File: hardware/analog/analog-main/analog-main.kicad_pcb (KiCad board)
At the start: 2 copper layers, 3 parts

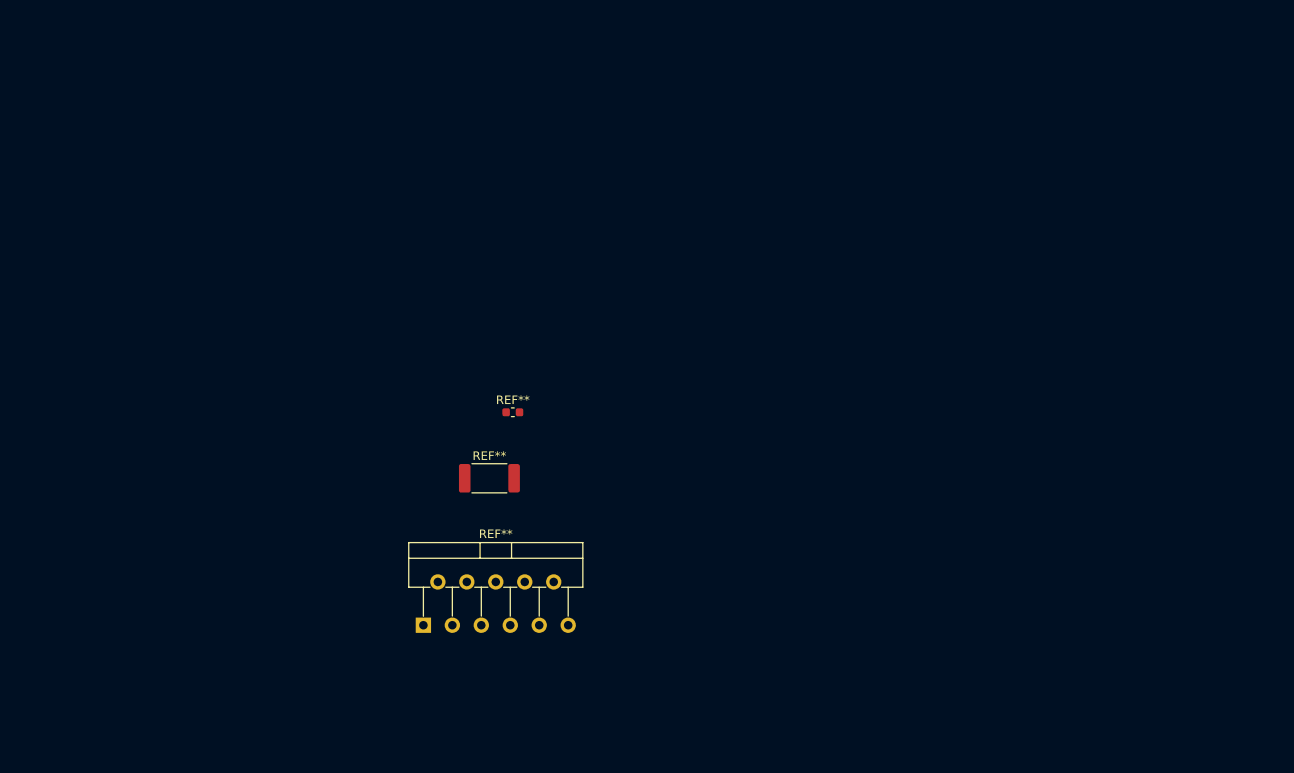
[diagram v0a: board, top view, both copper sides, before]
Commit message: Started work on Analog Main (Power Supply) board
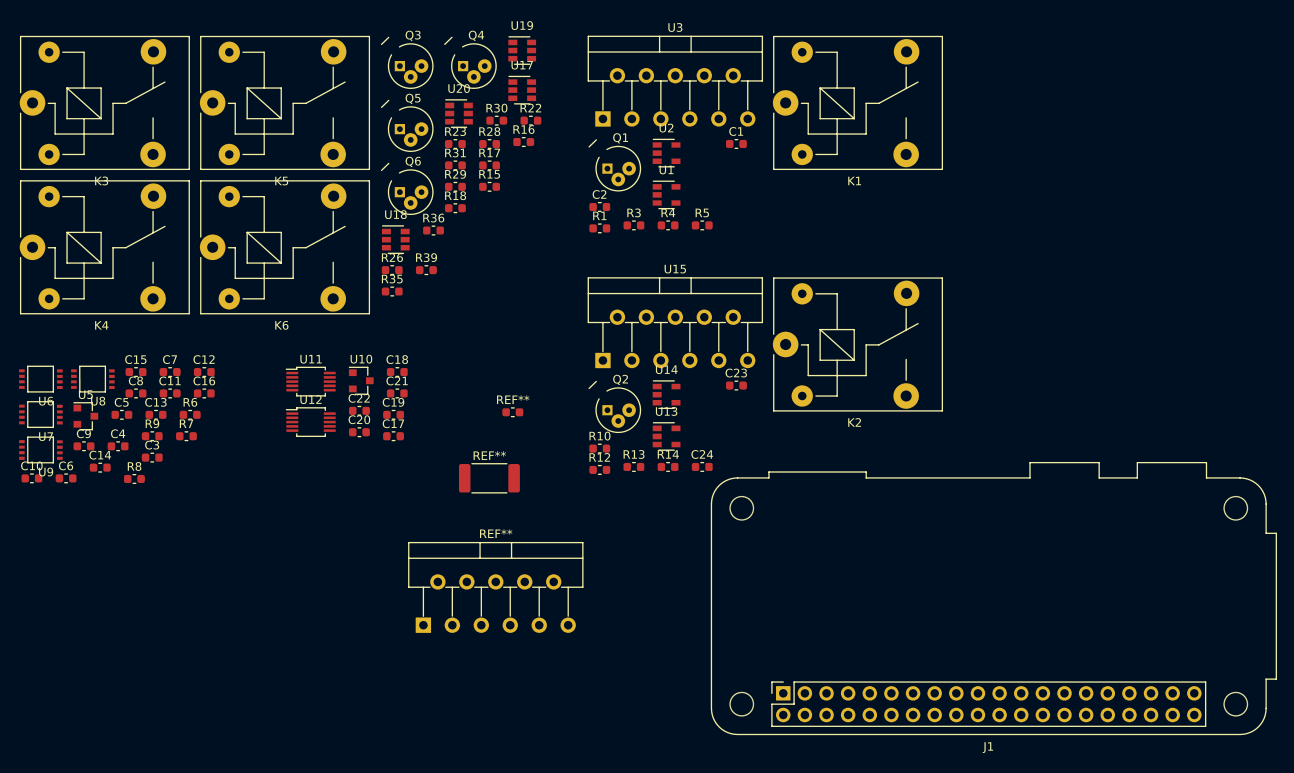
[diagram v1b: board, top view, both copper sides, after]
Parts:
- added C1: 100n, Capacitor_SMD:C_0603_1608Metric, F.Cu at (165.5, 46.5)
- added C10: 100n, Capacitor_SMD:C_0603_1608Metric, F.Cu at (82.8, 85.8)
- added C11: 100n / 100p, Capacitor_SMD:C_0603_1608Metric, F.Cu at (99.0, 75.8)
- added C12: 100n / 100p, Capacitor_SMD:C_0603_1608Metric, F.Cu at (103.0, 73.3)
- added C13: 4u7, Capacitor_SMD:C_0603_1608Metric, F.Cu at (97.4, 78.3)
- added C14: 4u7, Capacitor_SMD:C_0603_1608Metric, F.Cu at (90.8, 84.5)
- added C15: 100n, Capacitor_SMD:C_0603_1608Metric, F.Cu at (95.0, 73.3)
- added C16: 100n, Capacitor_SMD:C_0603_1608Metric, F.Cu at (103.0, 75.8)
- added C17: 100n, Capacitor_SMD:C_0603_1608Metric, F.Cu at (125.2, 80.8)
- added C18: 100n, Capacitor_SMD:C_0603_1608Metric, F.Cu at (125.7, 73.3)
- added C19: 100n, Capacitor_SMD:C_0603_1608Metric, F.Cu at (125.2, 78.3)
- added C2: 100n, Capacitor_SMD:C_0603_1608Metric, F.Cu at (149.5, 53.9)
- added C20: 100n, Capacitor_SMD:C_0603_1608Metric, F.Cu at (121.2, 80.3)
- added C21: 100n, Capacitor_SMD:C_0603_1608Metric, F.Cu at (125.7, 75.8)
- added C22: 100n, Capacitor_SMD:C_0603_1608Metric, F.Cu at (121.2, 77.8)
- added C23: 100n, Capacitor_SMD:C_0603_1608Metric, F.Cu at (165.5, 74.9)
- added C24: 100n, Capacitor_SMD:C_0603_1608Metric, F.Cu at (161.5, 84.4)
- added C3: 100n / 100p, Capacitor_SMD:C_0603_1608Metric, F.Cu at (96.9, 83.3)
- added C4: 100n / 100p, Capacitor_SMD:C_0603_1608Metric, F.Cu at (92.9, 82.0)
- added C5: 100n, Capacitor_SMD:C_0603_1608Metric, F.Cu at (93.3, 78.3)
- added C6: 4u7, Capacitor_SMD:C_0603_1608Metric, F.Cu at (86.8, 85.8)
- added C7: 4u7, Capacitor_SMD:C_0603_1608Metric, F.Cu at (99.0, 73.3)
- added C8: 100n, Capacitor_SMD:C_0603_1608Metric, F.Cu at (95.0, 75.8)
- added C9: 100n, Capacitor_SMD:C_0603_1608Metric, F.Cu at (88.9, 82.0)
- added J1: Raspberry_Pi_2_3, Module:Raspberry_Pi_Zero_Socketed_THT_FaceDown_MountingHoles, F.Cu at (171.0, 111.0)
- added K1: SANYOU_SRD_Form_C, Relay_THT:Relay_SPDT_SANYOU_SRD_Series_Form_C, F.Cu at (171.3, 41.7)
- added K2: SANYOU_SRD_Form_C, Relay_THT:Relay_SPDT_SANYOU_SRD_Series_Form_C, F.Cu at (171.3, 70.0)
- added K3: SANYOU_SRD_Form_C, Relay_THT:Relay_SPDT_SANYOU_SRD_Series_Form_C, F.Cu at (82.9, 41.7)
- added K4: SANYOU_SRD_Form_C, Relay_THT:Relay_SPDT_SANYOU_SRD_Series_Form_C, F.Cu at (82.9, 58.6)
- added K5: SANYOU_SRD_Form_C, Relay_THT:Relay_SPDT_SANYOU_SRD_Series_Form_C, F.Cu at (104.0, 41.7)
- added K6: SANYOU_SRD_Form_C, Relay_THT:Relay_SPDT_SANYOU_SRD_Series_Form_C, F.Cu at (104.0, 58.6)
- added Q1: 2N2222, digikey-footprints:TO-18-3, F.Cu at (150.4, 49.4)
- added Q2: 2N2222, digikey-footprints:TO-18-3, F.Cu at (150.4, 77.8)
- added Q3: 2N2222, digikey-footprints:TO-18-3, F.Cu at (126.0, 37.4)
- added Q4: 2N2222, digikey-footprints:TO-18-3, F.Cu at (133.4, 37.4)
- added Q5: 2N2222, digikey-footprints:TO-18-3, F.Cu at (126.0, 44.8)
- added Q6: 2N2222, digikey-footprints:TO-18-3, F.Cu at (126.0, 52.2)
- added R1: 1k, Resistor_SMD:R_0603_1608Metric, F.Cu at (149.5, 56.4)
- added R10: 1k, Resistor_SMD:R_0603_1608Metric, F.Cu at (149.5, 82.3)
- added R12: >250, Resistor_SMD:R_0603_1608Metric, F.Cu at (149.5, 84.8)
- added R13: 1k, Resistor_SMD:R_0603_1608Metric, F.Cu at (153.5, 84.4)
- added R14: 10k, Resistor_SMD:R_0603_1608Metric, F.Cu at (157.5, 84.4)
- added R15: 1k, Resistor_SMD:R_0603_1608Metric, F.Cu at (136.5, 51.5)
- added R16: 10k, Resistor_SMD:R_0603_1608Metric, F.Cu at (140.5, 46.3)
- added R17: 1k, Resistor_SMD:R_0603_1608Metric, F.Cu at (136.5, 49.0)
- added R18: 10k, Resistor_SMD:R_0603_1608Metric, F.Cu at (132.5, 54.0)
- added R22: 100R, Resistor_SMD:R_0603_1608Metric, F.Cu at (141.4, 43.8)
- added R23: 1k, Resistor_SMD:R_0603_1608Metric, F.Cu at (132.5, 46.5)
- added R26: 1k, Resistor_SMD:R_0603_1608Metric, F.Cu at (125.1, 61.3)
- added R28: 1k, Resistor_SMD:R_0603_1608Metric, F.Cu at (136.5, 46.5)
- added R29: 10k, Resistor_SMD:R_0603_1608Metric, F.Cu at (132.5, 51.5)
- added R3: >250, Resistor_SMD:R_0603_1608Metric, F.Cu at (153.5, 56.1)
- added R30: 1k, Resistor_SMD:R_0603_1608Metric, F.Cu at (137.4, 43.8)
- added R31: 10k, Resistor_SMD:R_0603_1608Metric, F.Cu at (132.5, 49.0)
- added R35: 100R, Resistor_SMD:R_0603_1608Metric, F.Cu at (125.1, 63.8)
- added R36: 1k, Resistor_SMD:R_0603_1608Metric, F.Cu at (129.9, 56.7)
- added R39: 1k, Resistor_SMD:R_0603_1608Metric, F.Cu at (129.1, 61.3)
- added R4: 1k, Resistor_SMD:R_0603_1608Metric, F.Cu at (157.5, 56.1)
- added R5: 10k, Resistor_SMD:R_0603_1608Metric, F.Cu at (161.5, 56.1)
- added R6: 10k, Resistor_SMD:R_0603_1608Metric, F.Cu at (101.4, 78.3)
- added R7: 10k, Resistor_SMD:R_0603_1608Metric, F.Cu at (100.9, 80.8)
- added R8: 10k, Resistor_SMD:R_0603_1608Metric, F.Cu at (94.8, 85.8)
- added R9: 10k, Resistor_SMD:R_0603_1608Metric, F.Cu at (96.9, 80.8)
- added U1: LMV321, Package_TO_SOT_SMD:SOT-23-5, F.Cu at (157.3, 52.5)
- added U10: MCP1525-TT, Package_TO_SOT_SMD:SOT-23, F.Cu at (121.5, 74.3)
- added U11: MCP3301, Package_SO:MSOP-10_3x3mm_P0.5mm, F.Cu at (115.6, 74.4)
- added U12: MCP3301, Package_SO:MSOP-10_3x3mm_P0.5mm, F.Cu at (115.6, 79.2)
- added U13: LMV321, Package_TO_SOT_SMD:SOT-23-5, F.Cu at (157.3, 80.8)
- added U14: LMV321, Package_TO_SOT_SMD:SOT-23-5, F.Cu at (157.3, 75.9)
- added U15: OPA549, Package_TO_SOT_THT:TO-220-11_P3.4x5.08mm_StaggerOdd_Lead4.85mm_Vertical, F.Cu at (149.8, 71.9)
- added U17: MAX4239AUT, Package_TO_SOT_SMD:SOT-23-6, F.Cu at (140.3, 40.2)
- added U18: MAX4239AUT, Package_TO_SOT_SMD:SOT-23-6, F.Cu at (125.5, 57.7)
- added U19: MAX4239AUT, Package_TO_SOT_SMD:SOT-23-6, F.Cu at (140.3, 35.5)
- added U2: LMV321, Package_TO_SOT_SMD:SOT-23-5, F.Cu at (157.3, 47.6)
- added U20: MAX4239AUT, Package_TO_SOT_SMD:SOT-23-6, F.Cu at (132.9, 42.9)
- added U3: OPA549, Package_TO_SOT_THT:TO-220-11_P3.4x5.08mm_StaggerOdd_Lead4.85mm_Vertical, F.Cu at (149.8, 43.6)
- added U5: MCP1525-TT, Package_TO_SOT_SMD:SOT-23, F.Cu at (89.1, 78.5)
- added U6: MAX5216, athir:uMAX8, F.Cu at (83.8, 74.1)
- added U7: MAX5216, athir:uMAX8, F.Cu at (83.8, 78.3)
- added U8: MAX5216, athir:uMAX8, F.Cu at (89.9, 74.1)
- added U9: MAX5216, athir:uMAX8, F.Cu at (83.8, 82.4)

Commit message: Applied fixed symbol for OPA549
Configured all footprints
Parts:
- removed REF**: C_0603_1608Metric, Capacitor_SMD:C_0603_1608Metric
- removed REF**: R_2512_6332Metric, Resistor_SMD:R_2512_6332Metric
- removed REF**: TO-220-11_P3.4x5.08mm_StaggerOdd_Lead4.85mm_Vertical, Package_TO_SOT_THT:TO-220-11_P3.4x5.08mm_StaggerOdd_Lead4.85mm_Vertical
- added C25: 100n, Capacitor_SMD:C_0603_1608Metric, F.Cu at (208.2, 129.2)
- added D1: TEMP_LED, LED_THT:LED_D5.0mm, F.Cu at (208.7, 112.8)
- added D2: D_Zener, Diode_THT:D_DO-35_SOD27_P7.62mm_Horizontal, F.Cu at (197.1, 110.6)
- added D3: TEMP_LED, LED_THT:LED_D5.0mm, F.Cu at (209.1, 124.2)
- added D4: D_Zener, Diode_THT:D_DO-35_SOD27_P7.62mm_Horizontal, F.Cu at (197.1, 128.7)
- added D5: D_Zener, Diode_THT:D_DO-35_SOD27_P7.62mm_Horizontal, F.Cu at (162.2, 66.0)
- added D6: D_Zener, Diode_THT:D_DO-35_SOD27_P7.62mm_Horizontal, F.Cu at (173.0, 62.4)
- added D7: D_Zener, Diode_THT:D_DO-35_SOD27_P7.62mm_Horizontal, F.Cu at (162.2, 62.4)
- added D8: D_Zener, Diode_THT:D_DO-35_SOD27_P7.62mm_Horizontal, F.Cu at (162.2, 69.5)
- added R11: 10k POT, Potentiometer_THT:Potentiometer_Bourns_3296W_Vertical, F.Cu at (203.6, 123.7)
- added R19: 10m 1%, Resistor_SMD:R_0603_1608Metric, F.Cu at (178.7, 70.5)
- added R2: 10k POT, Potentiometer_THT:Potentiometer_Bourns_3296W_Vertical, F.Cu at (203.6, 105.6)
- added R20: 10R 1%, Resistor_SMD:R_0603_1608Metric, F.Cu at (181.5, 68.0)
- added R21: 10k 1%, Resistor_SMD:R_0603_1608Metric, F.Cu at (174.7, 73.0)
- added R24: 6k8 1%, Resistor_SMD:R_0603_1608Metric, F.Cu at (181.5, 65.5)
- added R25: 2k2 1%, Resistor_SMD:R_0603_1608Metric, F.Cu at (173.4, 65.5)
- added R27: 3k 1%, Resistor_SMD:R_0603_1608Metric, F.Cu at (174.7, 70.5)
- added R32: 10m 1%, Resistor_SMD:R_0603_1608Metric, F.Cu at (177.5, 68.0)
- added R33: 10R 1%, Resistor_SMD:R_0603_1608Metric, F.Cu at (173.4, 68.0)
- added R34: 10k 1%, Resistor_SMD:R_0603_1608Metric, F.Cu at (177.5, 65.5)
- added R37: 6k8 1%, Resistor_SMD:R_0603_1608Metric, F.Cu at (170.7, 72.6)
- added R38: 2k2 1%, Resistor_SMD:R_0603_1608Metric, F.Cu at (166.7, 72.6)
- added R40: 3k 1%, Resistor_SMD:R_0603_1608Metric, F.Cu at (162.7, 72.6)
- added U4: 74HCT04, Package_SO:TSSOP-14_4.4x5mm_P0.65mm, F.Cu at (211.1, 105.7)
- moved C23 78.6 mm to (244.0, 71.4)
- moved C24 78.6 mm to (240.0, 80.9)
- moved K2 78.6 mm to (249.8, 66.5)
- moved Q2 78.6 mm to (228.9, 74.3)
- moved R10 78.6 mm to (228.0, 78.8)
- moved R12 78.6 mm to (228.0, 81.3)
- moved R13 78.6 mm to (232.0, 80.9)
- moved R14 78.6 mm to (236.0, 80.9)
- moved U13 78.6 mm to (235.8, 77.3)
- moved U14 78.6 mm to (235.8, 72.4)
- moved U15 78.6 mm to (228.3, 68.4)
- moved J1 54.3 mm to (120.0, 129.5)
- moved C1 51.6 mm to (216.8, 40.2)
- moved C2 51.6 mm to (200.7, 47.6)
- moved K1 51.6 mm to (222.5, 35.4)
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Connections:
- K1 pad 1: (no net) -> Net-(K1-Pad1)
- K2 pad 1: (no net) -> Net-(K2-Pad1)
- K4 pad 3: (no net) -> Net-(K4-Pad3)
- K4 pad 4: (no net) -> Net-(K4-Pad4)
- K6 pad 3: (no net) -> Net-(K6-Pad3)
- K6 pad 4: (no net) -> Net-(K6-Pad4)
- R12 pad 1: (no net) -> Net-(R12-Pad1)
- R12 pad 2: (no net) -> Net-(D3-Pad2)
- R3 pad 1: (no net) -> Net-(R3-Pad1)
- R3 pad 2: (no net) -> Net-(D1-Pad2)
- U15 pad 1: (no net) -> Net-(K2-Pad1)
- U15 pad 10: (no net) -> +36V
- U15 pad 11: (no net) -> +36V
- U15 pad 2: (no net) -> Net-(K2-Pad1)
- U15 pad 5: (no net) -> GND
- U15 pad 7: (no net) -> GND
- U15 pad 9: (no net) -> Net-(U15-Pad9)
- U3 pad 1: (no net) -> Net-(K1-Pad1)
- U3 pad 10: (no net) -> +36V
- U3 pad 11: (no net) -> +36V
- U3 pad 2: (no net) -> Net-(K1-Pad1)
- U3 pad 5: (no net) -> GND
- U3 pad 7: (no net) -> GND
- U3 pad 9: (no net) -> Net-(U3-Pad9)

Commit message: Sorry future me
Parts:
- removed R26: 1k, Resistor_SMD:R_0603_1608Metric
- removed R27: 3k 1%, Resistor_SMD:R_0603_1608Metric
- removed U18: MAX4239AUT, Package_TO_SOT_SMD:SOT-23-6
- added C26: 4700u, Capacitor_THT:CP_Radial_D26.0mm_P10.00mm_SnapIn, F.Cu at (68.0, -18.5)
- added C27: 4700u, Capacitor_THT:CP_Radial_D26.0mm_P10.00mm_SnapIn, F.Cu at (68.0, 9.05)
- added C28: 4700u, Capacitor_THT:CP_Radial_D26.0mm_P10.00mm_SnapIn, F.Cu at (96.4, -18.5)
- added C29: 4700u, Capacitor_THT:CP_Radial_D26.0mm_P10.00mm_SnapIn, F.Cu at (96.4, 9.05)
- added C30: 4700u, Capacitor_THT:CP_Radial_D26.0mm_P10.00mm_SnapIn, F.Cu at (256.2, 79.8)
- added C31: 4700u, Capacitor_THT:CP_Radial_D26.0mm_P10.00mm_SnapIn, F.Cu at (221.0, -19.8)
- added C32: 4700u, Capacitor_THT:CP_Radial_D26.0mm_P10.00mm_SnapIn, F.Cu at (187.4, -5.29)
- added C33: 4700u, Capacitor_THT:CP_Radial_D26.0mm_P10.00mm_SnapIn, F.Cu at (215.7, 7.80)
- added C34: 4700u, Capacitor_THT:CP_Radial_D26.0mm_P10.00mm_SnapIn, F.Cu at (249.4, -19.8)
- added C35: 4700u, Capacitor_THT:CP_Radial_D26.0mm_P10.00mm_SnapIn, F.Cu at (256.2, 110.7)
- added D10: D_Bridge_+-AA, Diode_THT:Diode_Bridge_32.0x5.6x17.0mm_P10.0mm_P7.5mm, F.Cu at (182.1, -22.6)
- added D9: D_Bridge_+-AA, Diode_THT:Diode_Bridge_32.0x5.6x17.0mm_P10.0mm_P7.5mm, F.Cu at (182.1, -29.9)
- R19, R32: value 10m 1% -> 100m 1%
- R20, R33: value 10R 1% -> 5R 1%
- R22: value 100R -> 10k 1%
- R23: value 1k -> 1k 1%
- R24: value 6k8 1% -> 33k 1%
- R25: value 2k2 1% -> 1k 1%
- moved C24 173.1 mm to (67.6, 96.0), turned to 270 degrees
- moved K2 172.3 mm to (82.0, 105.8), turned to 270 degrees
- moved C23 169.3 mm to (77.1, 100.0), turned to 270 degrees
- moved R14 168.8 mm to (67.6, 92.0), turned to 270 degrees
- moved U13 165.3 mm to (71.2, 91.8), turned to 270 degrees
- moved R13 164.5 mm to (67.6, 88.0), turned to 270 degrees
- moved U14 160.9 mm to (76.1, 91.8), turned to 270 degrees
- moved R12 160.8 mm to (67.2, 84.0), turned to 270 degrees
- moved R10 158.3 mm to (69.7, 84.0), turned to 270 degrees
- moved Q2 155.0 mm to (74.2, 84.9), turned to 270 degrees
- moved U15 149.1 mm to (80.1, 84.3), turned to 270 degrees
- moved D1 111.7 mm to (97.2, 119.8), turned to 270 degrees
- moved J1 109.8 mm to (35.0, 60.0), turned to 0 degrees
- moved R2 106.1 mm to (97.9, 114.6), turned to 270 degrees
- moved D2 104.2 mm to (92.9, 108.0), turned to 270 degrees
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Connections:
- R24 pad 1: Net-(R24-Pad1) -> (no net)
- R25 pad 1: Net-(R25-Pad1) -> GND
- R25 pad 2: Net-(R24-Pad1) -> Net-(R22-Pad1)
- U17 pad 1: Net-(R25-Pad1) -> /Analog to Digital/AIN0+
- U17 pad 2: -5V -> GND
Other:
- board outline added: 200 x 100 mm
